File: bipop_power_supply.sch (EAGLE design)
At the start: 19 parts, among them IC1 LM1117MP-3.3, IC2 LM1117MP-5.0

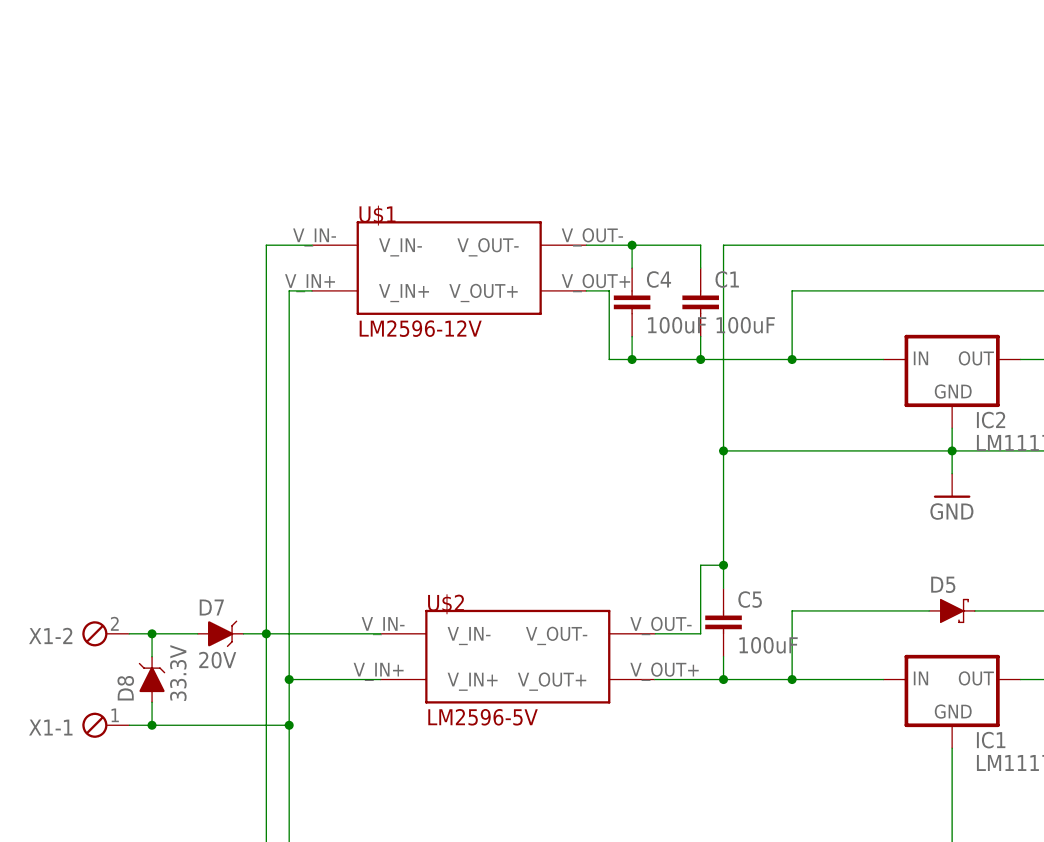
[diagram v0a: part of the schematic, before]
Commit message: .sch z diodami i kondensatorami, .brd TODO
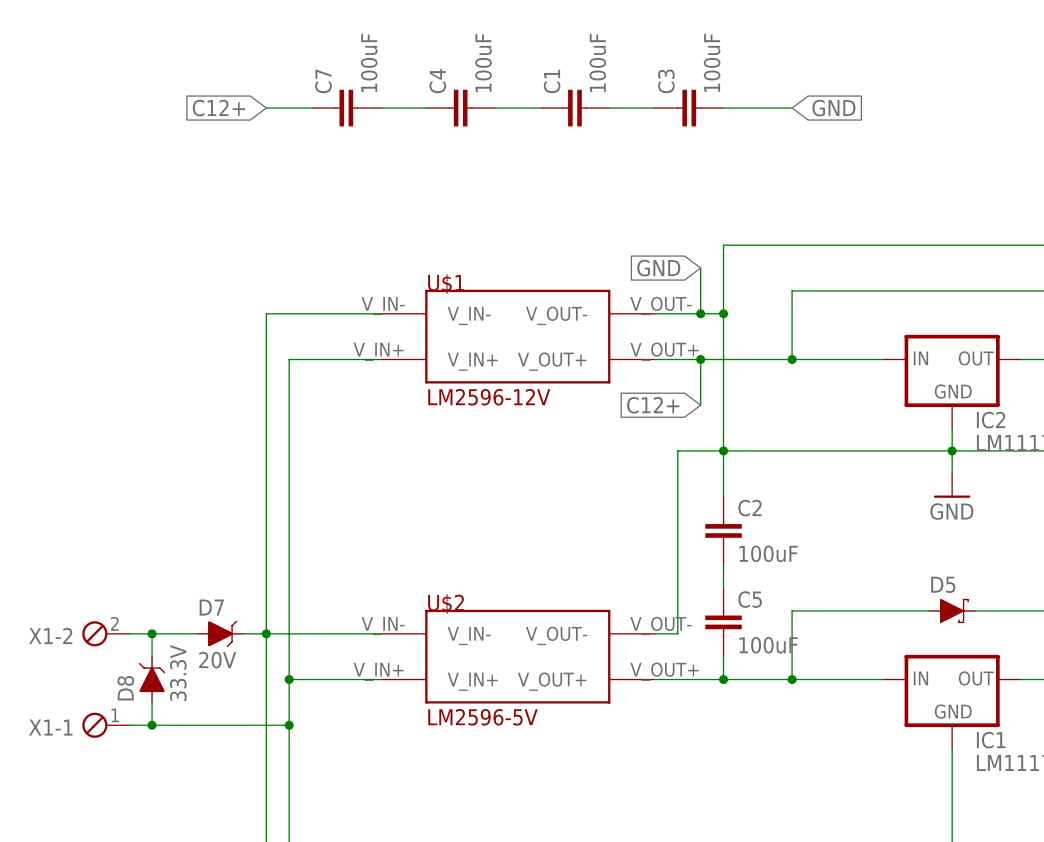
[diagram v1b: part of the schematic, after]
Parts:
- added C2, C3, C7: 100uF, rcl:C-EUC0805
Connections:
- removed net N$2: C1.2, C4.2, IC2.IN, U$1.V_OUT+, X4-2.1
- removed net N$6: C1.1, C4.1, U$1.V_OUT-
- new net C12+: C7.1, IC2.IN, U$1.V_OUT+, X4-2.1
- new net N$10: C1.1, C4.2
- new net N$12: C1.2, C3.1
- new net N$8: C2.2, C5.1
- new net N$9: C4.1, C7.2
- net GND: now also C2.1, C3.2, U$1.V_OUT-; no longer C5.1
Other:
- moved on the sheet: C1, C4, U$1
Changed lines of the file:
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@@
 <part name="C5" library="rcl" library_urn="urn:adsk.eagle:library:334" deviceset="C-EU" device="C0805" package3d_urn="urn:adsk.eagle:package:23617/2" value="100uF"/>
 <part name="C6" library="rcl" library_urn="urn:adsk.eagle:library:334" deviceset="C-EU" device="C0805" package3d_urn="urn:adsk.eagle:package:23617/2" value="100uF"/>
+<part name="C2" library="rcl" library_urn="urn:adsk.eagle:library:334" deviceset="C-EU" device="C0805" package3d_urn="urn:adsk.eagle:package:23617/2" value="100uF"/>
+<part name="C3" library="rcl" library_urn="urn:adsk.eagle:library:334" deviceset="C-EU" device="C0805" package3d_urn="urn:adsk.eagle:package:23617/2" value="100uF"/>
+<part name="C7" library="rcl" library_urn="urn:adsk.eagle:library:334" deviceset="C-EU" device="C0805" package3d_urn="urn:adsk.eagle:package:23617/2" value="100uF"/>
 </parts>
 <sheets>
@@
 <instance part="X1" gate="-1" x="-17.78" y="12.7" rot="R180"/>
 <instance part="X1" gate="-2" x="-17.78" y="22.86" rot="R180"/>
-<instance part="U$1" gate="G$1" x="20.32" y="63.5"/>
+<instance part="U$1" gate="G$1" x="27.94" y="55.88"/>
 <instance part="U$2" gate="G$1" x="27.94" y="20.32"/>
 <instance part="U$3" gate="G$1" x="27.94" y="-7.62"/>
@@
 <instance part="FRAME1" gate="G$2" x="48.26" y="-101.6"/>
 <instance part="D7" gate="G$1" x="-5.08" y="22.86"/>
-<instance part="C1" gate="G$1" x="48.26" y="60.96"/>
+<instance part="C1" gate="G$1" x="33.02" y="81.28" rot="R90"/>
 <instance part="D8" gate="G$1" x="-12.7" y="17.78" rot="R90"/>
-<instance part="C4" gate="G$1" x="40.64" y="60.96"/>
+<instance part="C4" gate="G$1" x="20.32" y="81.28" rot="R90"/>
 <instance part="C5" gate="G$1" x="50.8" y="25.4"/>
 <instance part="C6" gate="G$1" x="50.8" y="-10.16"/>
+<instance part="C2" gate="G$1" x="50.8" y="35.56"/>
+<instance part="C3" gate="G$1" x="45.72" y="81.28" rot="R90"/>
+<instance part="C7" gate="G$1" x="7.62" y="81.28" rot="R90"/>
 </instances>
 <busses>
 </busses>
 <nets>
-<net name="N$2" class="0">
-<segment>
-<wire x1="124.46" y1="60.96" x2="58.42" y2="60.96" width="0.1524" layer="91"/>
-<wire x1="58.42" y1="60.96" x2="58.42" y2="53.34" width="0.1524" layer="91"/>
-<wire x1="68.58" y1="53.34" x2="58.42" y2="53.34" width="0.1524" layer="91"/>
-<junction x="58.42" y="53.34"/>
-<pinref part="X4" gate="-2" pin="1"/>
-<wire x1="132.08" y1="35.56" x2="124.46" y2="35.56" width="0.1524" layer="91"/>
-<wire x1="124.46" y1="35.56" x2="124.46" y2="60.96" width="0.1524" layer="91"/>
-<wire x1="58.42" y1="53.34" x2="48.26" y2="53.34" width="0.1524" layer="91"/>
-<pinref part="IC2" gate="G$1" pin="IN"/>
-<pinref part="C1" gate="G$1" pin="2"/>
-<wire x1="48.26" y1="55.88" x2="48.26" y2="53.34" width="0.1524" layer="91"/>
-<pinref part="C4" gate="G$1" pin="2"/>
-<wire x1="40.64" y1="55.88" x2="40.64" y2="53.34" width="0.1524" layer="91"/>
-<wire x1="40.64" y1="53.34" x2="48.26" y2="53.34" width="0.1524" layer="91"/>
-<junction x="48.26" y="53.34"/>
-<wire x1="40.64" y1="53.34" x2="38.1" y2="53.34" width="0.1524" layer="91"/>
-<wire x1="38.1" y1="53.34" x2="38.1" y2="60.96" width="0.1524" layer="91"/>
-<junction x="40.64" y="53.34"/>
-<pinref part="U$1" gate="G$1" pin="V_OUT+"/>
-<wire x1="38.1" y1="60.96" x2="35.56" y2="60.96" width="0.1524" layer="91"/>
-</segment>
-</net>
 <net name="GND" class="0">
 <segment>
@@
 <wire x1="129.54" y1="66.04" x2="50.8" y2="66.04" width="0.1524" layer="91"/>
 <junction x="76.2" y="43.18"/>
-<wire x1="50.8" y1="66.04" x2="50.8" y2="43.18" width="0.1524" layer="91"/>
+<wire x1="50.8" y1="66.04" x2="50.8" y2="58.42" width="0.1524" layer="91"/>
+<wire x1="50.8" y1="58.42" x2="50.8" y2="43.18" width="0.1524" layer="91"/>
 <wire x1="76.2" y1="43.18" x2="50.8" y2="43.18" width="0.1524" layer="91"/>
 <wire x1="119.38" y1="43.18" x2="76.2" y2="43.18" width="0.1524" layer="91"/>
@@
 <wire x1="119.38" y1="30.48" x2="119.38" y2="43.18" width="0.1524" layer="91"/>
 <pinref part="IC2" gate="G$1" pin="GND"/>
-<pinref part="C5" gate="G$1" pin="1"/>
-<wire x1="50.8" y1="27.94" x2="50.8" y2="30.48" width="0.1524" layer="91"/>
+<pinref part="C2" gate="G$1" pin="1"/>
+<wire x1="50.8" y1="38.1" x2="50.8" y2="43.18" width="0.1524" layer="91"/>
 <junction x="50.8" y="43.18"/>
 <pinref part="U$2" gate="G$1" pin="V_OUT-"/>
-<wire x1="50.8" y1="30.48" x2="50.8" y2="43.18" width="0.1524" layer="91"/>
-<wire x1="43.18" y1="22.86" x2="48.26" y2="22.86" width="0.1524" layer="91"/>
-<wire x1="48.26" y1="22.86" x2="48.26" y2="30.48" width="0.1524" layer="91"/>
-<wire x1="48.26" y1="30.48" x2="50.8" y2="30.48" width="0.1524" layer="91"/>
-<junction x="50.8" y="30.48"/>
+<wire x1="43.18" y1="22.86" x2="45.72" y2="22.86" width="0.1524" layer="91"/>
+<wire x1="45.72" y1="22.86" x2="45.72" y2="43.18" width="0.1524" layer="91"/>
+<wire x1="45.72" y1="43.18" x2="50.8" y2="43.18" width="0.1524" layer="91"/>
+<pinref part="U$1" gate="G$1" pin="V_OUT-"/>
+<wire x1="43.18" y1="58.42" x2="48.26" y2="58.42" width="0.1524" layer="91"/>
+<junction x="50.8" y="58.42"/>
+<wire x1="48.26" y1="58.42" x2="50.8" y2="58.42" width="0.1524" layer="91"/>
+<wire x1="48.26" y1="58.42" x2="48.26" y2="63.5" width="0.1524" layer="91"/>
+<junction x="48.26" y="58.42"/>
+<label x="48.26" y="63.5" size="1.778" layer="95" rot="R180" xref="yes"/>
 </segment>
 <segment>
@@
 <junction x="50.8" y="-5.08"/>
 </segment>
+<segment>
+<pinref part="C3" gate="G$1" pin="2"/>
+<wire x1="50.8" y1="81.28" x2="58.42" y2="81.28" width="0.1524" layer="91"/>
+<label x="58.42" y="81.28" size="1.778" layer="95" xref="yes"/>
+</segment>
 </net>
 <net name="N$5" class="0">
@@
 <wire x1="12.7" y1="17.78" x2="2.54" y2="17.78" width="0.1524" layer="91"/>
 <junction x="2.54" y="17.78"/>
-<wire x1="5.08" y1="60.96" x2="2.54" y2="60.96" width="0.1524" layer="91"/>
-<wire x1="2.54" y1="60.96" x2="2.54" y2="17.78" width="0.1524" layer="91"/>
-<pinref part="U$1" gate="G$1" pin="V_IN+"/>
 <pinref part="U$2" gate="G$1" pin="V_IN+"/>
 <pinref part="U$3" gate="G$1" pin="V_IN+"/>
+<wire x1="2.54" y1="53.34" x2="2.54" y2="17.78" width="0.1524" layer="91"/>
 <wire x1="12.7" y1="-10.16" x2="2.54" y2="-10.16" width="0.1524" layer="91"/>
 <wire x1="2.54" y1="-10.16" x2="2.54" y2="12.7" width="0.1524" layer="91"/>
@@
 <wire x1="-12.7" y1="15.24" x2="-12.7" y2="12.7" width="0.1524" layer="91"/>
 <junction x="-12.7" y="12.7"/>
+<pinref part="U$1" gate="G$1" pin="V_IN+"/>
+<wire x1="12.7" y1="53.34" x2="2.54" y2="53.34" width="0.1524" layer="91"/>
 </segment>
 </net>
@@
 <pinref part="U$2" gate="G$1" pin="V_IN-"/>
 <pinref part="U$3" gate="G$1" pin="V_IN-"/>
+<pinref part="D7" gate="G$1" pin="C"/>
 <pinref part="U$1" gate="G$1" pin="V_IN-"/>
-<wire x1="5.08" y1="66.04" x2="0" y2="66.04" width="0.1524" layer="91"/>
-<wire x1="0" y1="66.04" x2="0" y2="22.86" width="0.1524" layer="91"/>
-<pinref part="D7" gate="G$1" pin="C"/>
+<wire x1="0" y1="58.42" x2="0" y2="22.86" width="0.1524" layer="91"/>
+<wire x1="12.7" y1="58.42" x2="0" y2="58.42" width="0.1524" layer="91"/>
 </segment>
 </net>
@@
 </segment>
 </net>
-<net name="N$6" class="0">
-<segment>
+<net name="N$8" class="0">
+<segment>
+<pinref part="C5" gate="G$1" pin="1"/>
+<pinref part="C2" gate="G$1" pin="2"/>
+<wire x1="50.8" y1="27.94" x2="50.8" y2="30.48" width="0.1524" layer="91"/>
+</segment>
+</net>
+<net name="C12+" class="0">
+<segment>
+<pinref part="C7" gate="G$1" pin="1"/>
+<wire x1="5.08" y1="81.28" x2="0" y2="81.28" width="0.1524" layer="91"/>
+<label x="0" y="81.28" size="1.778" layer="95" rot="R180" xref="yes"/>
+</segment>
+<segment>
+<wire x1="124.46" y1="60.96" x2="58.42" y2="60.96" width="0.1524" layer="91"/>
+<wire x1="58.42" y1="60.96" x2="58.42" y2="53.34" width="0.1524" layer="91"/>
+<wire x1="68.58" y1="53.34" x2="58.42" y2="53.34" width="0.1524" layer="91"/>
+<pinref part="X4" gate="-2" pin="1"/>
+<wire x1="132.08" y1="35.56" x2="124.46" y2="35.56" width="0.1524" layer="91"/>
+<wire x1="124.46" y1="35.56" x2="124.46" y2="60.96" width="0.1524" layer="91"/>
+<pinref part="IC2" gate="G$1" pin="IN"/>
+<pinref part="U$1" gate="G$1" pin="V_OUT+"/>
+<wire x1="43.18" y1="53.34" x2="48.26" y2="53.34" width="0.1524" layer="91"/>
+<junction x="58.42" y="53.34"/>
+<wire x1="48.26" y1="53.34" x2="58.42" y2="53.34" width="0.1524" layer="91"/>
+<wire x1="48.26" y1="53.34" x2="48.26" y2="48.26" width="0.1524" layer="91"/>
+<junction x="48.26" y="53.34"/>
+<label x="48.26" y="48.26" size="1.778" layer="95" rot="R180" xref="yes"/>
+</segment>
+</net>
+<net name="N$9" class="0">
+<segment>
+<pinref part="C7" gate="G$1" pin="2"/>
+<pinref part="C4" gate="G$1" pin="1"/>
+<wire x1="12.7" y1="81.28" x2="17.78" y2="81.28" width="0.1524" layer="91"/>
+</segment>
+</net>
+<net name="N$10" class="0">
+<segment>
+<pinref part="C4" gate="G$1" pin="2"/>
 <pinref part="C1" gate="G$1" pin="1"/>
-<wire x1="48.26" y1="63.5" x2="48.26" y2="66.04" width="0.1524" layer="91"/>
-<pinref part="U$1" gate="G$1" pin="V_OUT-"/>
-<wire x1="48.26" y1="66.04" x2="40.64" y2="66.04" width="0.1524" layer="91"/>
-<pinref part="C4" gate="G$1" pin="1"/>
-<wire x1="40.64" y1="66.04" x2="35.56" y2="66.04" width="0.1524" layer="91"/>
-<wire x1="40.64" y1="63.5" x2="40.64" y2="66.04" width="0.1524" layer="91"/>
-<junction x="40.64" y="66.04"/>
-</segment>
-</net>
+<wire x1="25.4" y1="81.28" x2="30.48" y2="81.28" width="0.1524" layer="91"/>
+</segment>
+</net>
+<net name="N$12" class="0">
+<segment>
+<pinref part="C1" gate="G$1" pin="2"/>
+<pinref part="C3" gate="G$1" pin="1"/>
+<wire x1="38.1" y1="81.28" x2="43.18" y2="81.28" width="0.1524" layer="91"/>
+</segment>
+</net>
